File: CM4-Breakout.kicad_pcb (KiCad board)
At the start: 2 copper layers, 9 parts, among them J1 Conn_01x35_Male, J2 Conn_01x33_Male, J3 Conn_01x33_Male, J4 Conn_01x35_Male, J5 Conn_01x02_Female, J6 Conn_01x04_Male

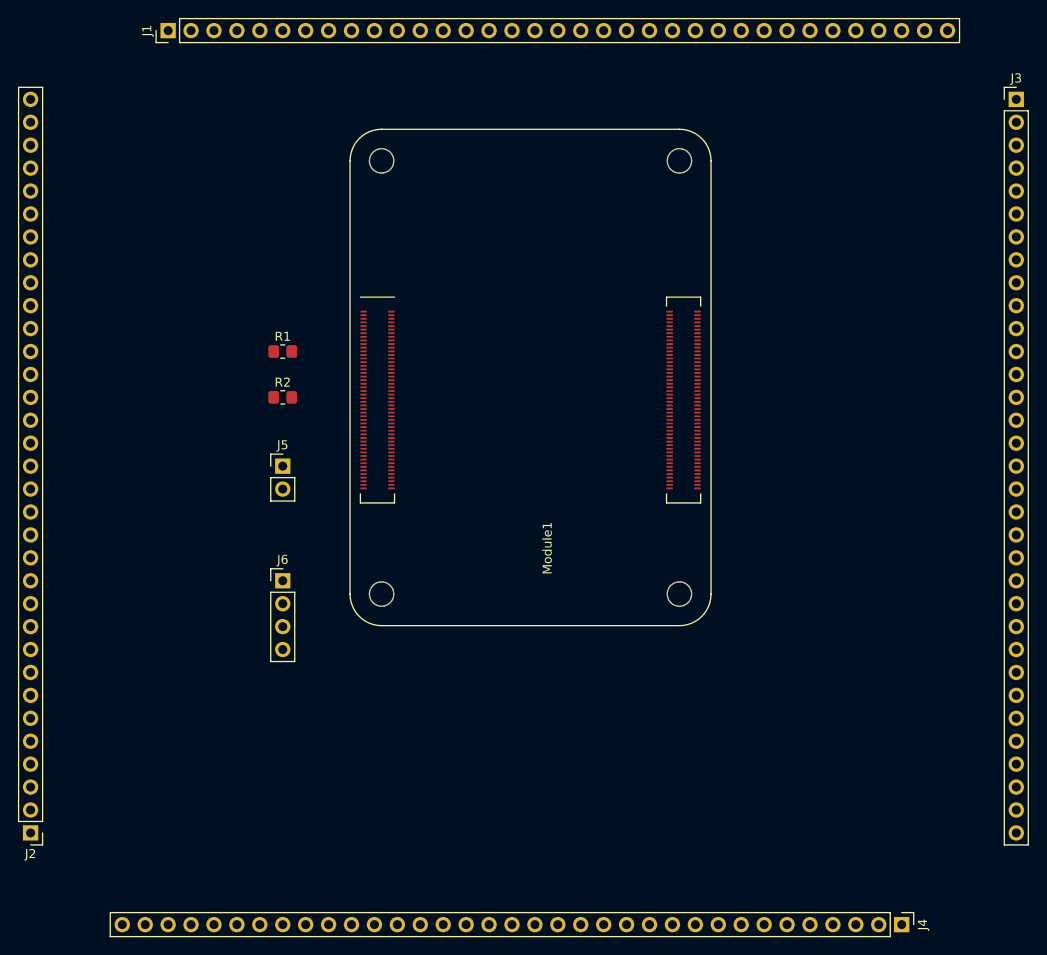
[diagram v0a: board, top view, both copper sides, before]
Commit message: Some updates to the pinout
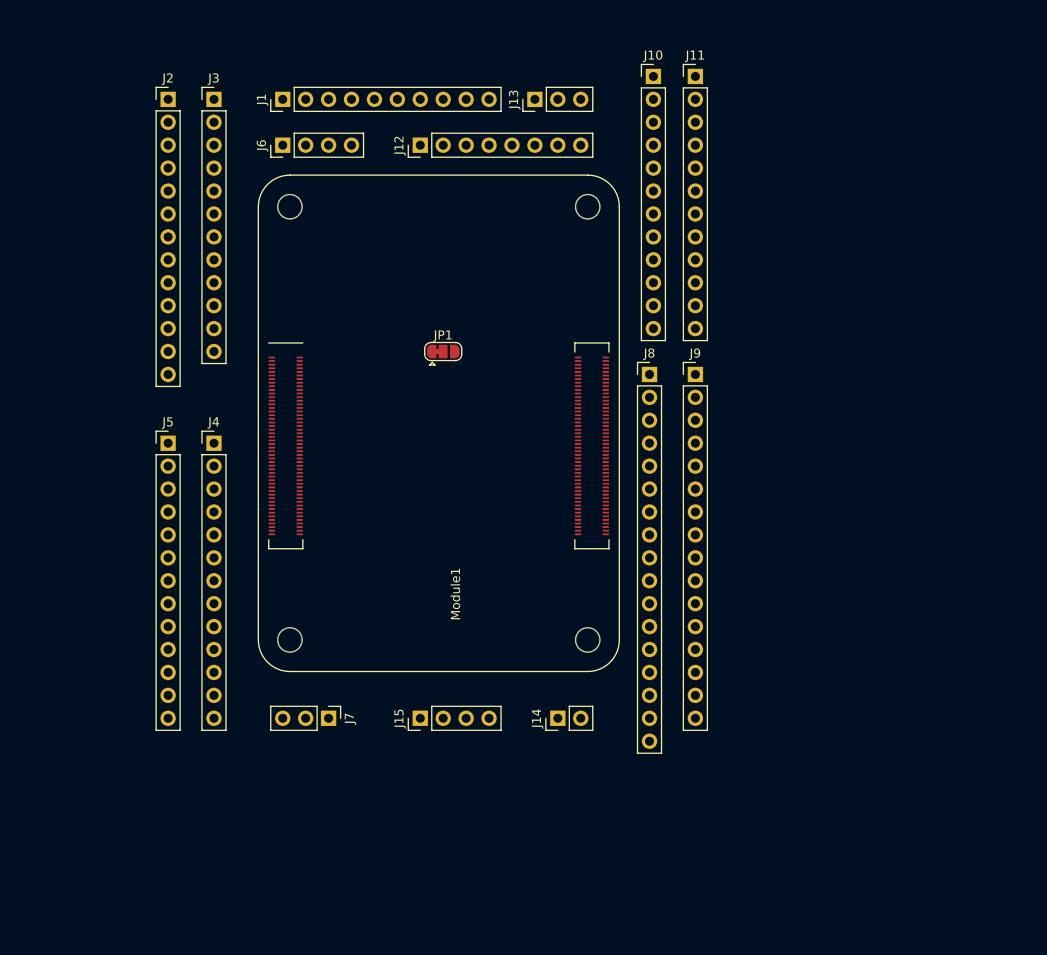
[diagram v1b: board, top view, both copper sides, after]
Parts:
- removed R1: 0R, Resistor_SMD:R_0805_2012Metric_Pad1.20x1.40mm_HandSolder
- removed R2: nf, Resistor_SMD:R_0805_2012Metric_Pad1.20x1.40mm_HandSolder
- added J10: Conn_01x12_Male, Connector_PinHeader_2.54mm:PinHeader_1x12_P2.54mm_Vertical, F.Cu at (178.2, 55.9)
- added J11: Conn_01x12_Male, Connector_PinHeader_2.54mm:PinHeader_1x12_P2.54mm_Vertical, F.Cu at (182.9, 55.9)
- added J12: Conn_01x08_Male, Connector_PinHeader_2.54mm:PinHeader_1x08_P2.54mm_Vertical, F.Cu at (152.4, 63.5)
- added J13: Conn_01x03_Male, Connector_PinHeader_2.54mm:PinHeader_1x03_P2.54mm_Vertical, F.Cu at (165.1, 58.4)
- added J14: Conn_01x02_Female, Connector_PinHeader_2.54mm:PinHeader_1x02_P2.54mm_Vertical, F.Cu at (167.6, 127.0)
- added J15: Conn_01x04_Male, Connector_PinHeader_2.54mm:PinHeader_1x04_P2.54mm_Vertical, F.Cu at (152.4, 127.0)
- added J7: Conn_01x03_Male, Connector_PinHeader_2.54mm:PinHeader_1x03_P2.54mm_Vertical, F.Cu at (142.2, 127.0)
- added J8: Conn_01x17_Male, Connector_PinHeader_2.54mm:PinHeader_1x17_P2.54mm_Vertical, F.Cu at (177.8, 88.9)
- added J9: Conn_01x16_Male, Connector_PinHeader_2.54mm:PinHeader_1x16_P2.54mm_Vertical, F.Cu at (182.9, 88.9)
- added JP1: SolderJumper_3_Bridged12, Jumper:SolderJumper-3_P1.3mm_Bridged12_RoundedPad1.0x1.5mm, F.Cu at (154.9, 86.4)
- J1: value Conn_01x35_Male -> Conn_01x10_Male; footprint Connector_PinHeader_2.54mm:PinHeader_1x35_P2.54mm_Vertical -> Connector_PinHeader_2.54mm:PinHeader_1x10_P2.54mm_Vertical
- J2: value Conn_01x33_Male -> Conn_01x13_Male; footprint Connector_PinHeader_2.54mm:PinHeader_1x33_P2.54mm_Vertical -> Connector_PinHeader_2.54mm:PinHeader_1x13_P2.54mm_Vertical
- J3: value Conn_01x33_Male -> Conn_01x12_Male; footprint Connector_PinHeader_2.54mm:PinHeader_1x33_P2.54mm_Vertical -> Connector_PinHeader_2.54mm:PinHeader_1x12_P2.54mm_Vertical
- J4: value Conn_01x35_Male -> Conn_01x13_Male; footprint Connector_PinHeader_2.54mm:PinHeader_1x35_P2.54mm_Vertical -> Connector_PinHeader_2.54mm:PinHeader_1x13_P2.54mm_Vertical
- J5: value Conn_01x02_Female -> Conn_01x13_Male; footprint Connector_PinHeader_2.54mm:PinHeader_1x02_P2.54mm_Vertical -> Connector_PinHeader_2.54mm:PinHeader_1x13_P2.54mm_Vertical
- moved J4 93.0 mm to (129.5, 96.5), turned to 0 degrees
- moved J3 88.9 mm to (129.5, 58.4)
- moved J2 82.7 mm to (124.5, 58.4), turned to 0 degrees
- moved J6 48.3 mm to (137.2, 63.5), turned to 90 degrees
- moved J1 14.8 mm to (137.2, 58.4)
- moved J5 13.0 mm to (124.5, 96.5)
- moved Module1 11.4 mm to (138.0, 118.3)
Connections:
- J2 pad 1: /PI_LED_nPWR -> /Ethernet_Pair0_P
- J2 pad 10: /GPIO8 -> /Ethernet_nLED2
- J2 pad 11: /GPIO9 -> /Ethernet_nLED3
- J2 pad 12: /GPIO10 -> /Ethernet_SYNC_IN
- J2 pad 13: /GPIO11 -> /Ethernet_SYNC_OUT
- J2 pad 2: /Pi_nLED_Activity -> /Ethernet_Pair0_N
- J2 pad 3: /GPIO_VREF -> /Ethernet_Pair1_P
- J2 pad 4: /GPIO2 -> /Ethernet_Pair1_N
- J2 pad 5: /GPIO3 -> /Ethernet_Pair2_P
- J2 pad 6: /GPIO4 -> /Ethernet_Pair2_N
- J2 pad 7: /GPIO5 -> /Ethernet_Pair3_P
- J2 pad 8: /GPIO6 -> /Ethernet_Pair3_N
- J2 pad 9: /GPIO7 -> /Ethernet_nLED1
- J3 pad 1: /CAM0_C_N -> /SD_CLK
- J3 pad 10: /CAM1_D0_P -> /SD_DAT7
- J3 pad 11: /CAM1_D1_N -> /SD_VDD_Override
- J3 pad 12: /CAM1_D1_P -> /SD_PWR_ON
- J3 pad 2: /CAM0_C_P -> /SD_CMD
- J3 pad 3: /CAM0_D0_N -> /SD_DAT0
- J3 pad 4: /CAM0_D0_P -> /SD_DAT1
- J3 pad 5: /CAM0_D1_N -> /SD_DAT2
- J3 pad 6: /CAM0_D1_P -> /SD_DAT3
- J3 pad 7: /CAM1_C_N -> /SD_DAT4
- J3 pad 8: /CAM1_C_P -> /SD_DAT5
- J3 pad 9: /CAM1_D0_N -> /SD_DAT6
- J4 pad 1: /HDMI0_CEC -> /GPIO15
- J4 pad 10: /HDMI0_TX1_P -> /GPIO24
- J4 pad 11: /HDMI0_TX2_N -> /GPIO25
- J4 pad 12: /HDMI0_TX2_P -> /GPIO26
- J4 pad 13: /HDMI1_CEC -> /GPIO27
- J4 pad 2: /HDMI0_CLK_N -> /GPIO16
- J4 pad 3: /HDMI0_CLK_P -> /GPIO17
- J4 pad 4: /HDMI0_HOTPLUG -> /GPIO18
- J4 pad 5: /HDMI0_SCL -> /GPIO19
- J4 pad 6: /HDMI0_SDA -> /GPIO20
- J4 pad 7: /HDMI0_TX0_N -> /GPIO21
- J4 pad 8: /HDMI0_TX0_P -> /GPIO22
- J4 pad 9: /HDMI0_TX1_N -> /GPIO23
- J5 pad 1: /+5v -> /GPIO2
- J5 pad 2: /GND -> /GPIO3
- J6 pad 1: /+5v -> /ID_SC
- J6 pad 2: /+3.3v -> /ID_SD
- J6 pad 3: /+1.8v -> /SCL0
- J6 pad 4: /GND -> /SDA0

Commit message: Final
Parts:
- added J16: Conn_01x03_Male, Connector_PinHeader_2.54mm:PinHeader_1x03_P2.54mm_Vertical, F.Cu at (185.0, 127.4)
- added J17: Conn_01x02_Female, Connector_PinHeader_2.54mm:PinHeader_1x02_P2.54mm_Vertical, F.Cu at (120.0, 140.0)
- added J18: Conn_01x04_Male, Connector_PinHeader_2.54mm:PinHeader_1x04_P2.54mm_Vertical, F.Cu at (167.5, 127.5)
- J10: value Conn_01x12_Male -> Conn_01x10_Male; footprint Connector_PinHeader_2.54mm:PinHeader_1x12_P2.54mm_Vertical -> Connector_PinHeader_2.54mm:PinHeader_1x10_P2.54mm_Vertical
- J11: value Conn_01x12_Male -> Conn_01x06_Male; footprint Connector_PinHeader_2.54mm:PinHeader_1x12_P2.54mm_Vertical -> Connector_PinHeader_2.54mm:PinHeader_1x06_P2.54mm_Vertical
- J12: value Conn_01x08_Male -> Conn_01x10_Male; footprint Connector_PinHeader_2.54mm:PinHeader_1x08_P2.54mm_Vertical -> Connector_PinHeader_2.54mm:PinHeader_1x10_P2.54mm_Vertical
- J13: value Conn_01x03_Male -> Conn_01x12_Male; footprint Connector_PinHeader_2.54mm:PinHeader_1x03_P2.54mm_Vertical -> Connector_PinHeader_2.54mm:PinHeader_1x12_P2.54mm_Vertical
- J14: value Conn_01x02_Female -> Conn_01x12_Male; footprint Connector_PinHeader_2.54mm:PinHeader_1x02_P2.54mm_Vertical -> Connector_PinHeader_2.54mm:PinHeader_1x12_P2.54mm_Vertical
- J15: value Conn_01x04_Male -> Conn_01x08_Male; footprint Connector_PinHeader_2.54mm:PinHeader_1x04_P2.54mm_Vertical -> Connector_PinHeader_2.54mm:PinHeader_1x08_P2.54mm_Vertical
- J8: value Conn_01x17_Male -> Conn_01x01_Male; footprint Connector_PinHeader_2.54mm:PinHeader_1x17_P2.54mm_Vertical -> Connector_PinHeader_2.54mm:PinHeader_1x01_P2.54mm_Vertical
- J9: value Conn_01x16_Male -> Conn_01x06_Male; footprint Connector_PinHeader_2.54mm:PinHeader_1x16_P2.54mm_Vertical -> Connector_PinHeader_2.54mm:PinHeader_1x06_P2.54mm_Vertical
- moved J12 71.9 mm to (205.0, 112.5), turned to 0 degrees
- moved J15 61.1 mm to (185.0, 75.3), turned to 180 degrees
- moved J10 59.1 mm to (195.0, 112.5)
- moved J14 56.2 mm to (205.0, 85.0), turned to 180 degrees
- moved J8 46.7 mm to (185.0, 135.0)
- moved JP1 43.8 mm to (140.0, 127.5)
- moved J11 42.8 mm to (205.0, 92.5)
- moved J13 29.9 mm to (195.0, 57.4), turned to 0 degrees
- moved J1 15.4 mm to (152.5, 57.5)
- moved J7 15.3 mm to (157.5, 127.5)
- moved J9 12.6 mm to (195.0, 92.5)
- moved J3 9.58 mm to (120.0, 57.5)
- moved J6 6.00 mm to (137.2, 57.5)
- moved J5 4.46 mm to (120.0, 96.5)
- moved J2 3.01 mm to (127.3, 57.4)
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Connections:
- net Net-(Module1-Pad104) renamed no_connect_141
- net Net-(Module1-Pad106) renamed no_connect_142
- net Net-(Module1-Pad76) renamed no_connect_143
- J10 pad 1: /HDMI0_CEC -> /CAM1_C_N
- J10 pad 10: /HDMI0_TX1_P -> /CAM1_D3_P
- J10 pad 2: /HDMI0_CLK_N -> /CAM1_C_P
- J10 pad 3: /HDMI0_CLK_P -> /CAM1_D0_N
- J10 pad 4: /HDMI0_HOTPLUG -> /CAM1_D0_P
- J10 pad 5: /HDMI0_SCL -> /CAM1_D1_N
- J10 pad 6: /HDMI0_SDA -> /CAM1_D1_P
- J10 pad 7: /HDMI0_TX0_N -> /CAM1_D2_N
- J10 pad 8: /HDMI0_TX0_P -> /CAM1_D2_P
- J10 pad 9: /HDMI0_TX1_N -> /CAM1_D3_N
- J11 pad 1: /HDMI1_CEC -> /DSI0_C_N
- J11 pad 2: /HDMI1_CLK_N -> /DSI0_C_P
- J11 pad 3: /HDMI1_CLK_P -> /DSI0_D0_N
- J11 pad 4: /HDMI1_HOTPLUG -> /DSI0_D0_P
- J11 pad 5: /HDMI1_SCL -> /DSI0_D1_N
- J11 pad 6: /HDMI1_SDA -> /DSI0_D1_P
- J12 pad 1: /PCIe_CLK_nREQ -> /DSI1_C_N
- J12 pad 2: /PCIe_CLK_N -> /DSI1_C_P
- J12 pad 3: /PCIe_CLK_P -> /DSI1_D0_N
- J12 pad 4: /PCIe_nRST -> /DSI1_D0_P
- J12 pad 5: /PCIe_RX_N -> /DSI1_D1_N
- J12 pad 6: /PCIe_RX_P -> /DSI1_D1_P
- J12 pad 7: /PCIe_TX_N -> /DSI1_D2_N
- J12 pad 8: /PCIe_TX_P -> /DSI1_D2_P
- J13 pad 1: /USB_OTG_ID -> /HDMI0_CEC
- J13 pad 2: /USB2_N -> /HDMI0_CLK_N
- J13 pad 3: /USB2_P -> /HDMI0_CLK_P
- J14 pad 1: /+5v -> /HDMI1_CEC
- J14 pad 2: /GND -> /HDMI1_CLK_N
- J15 pad 1: /+5v -> /PCIe_CLK_nREQ
- J15 pad 2: /+3.3v -> /PCIe_CLK_N
- J15 pad 3: /+1.8v -> /PCIe_CLK_P
- J15 pad 4: /GND -> /PCIe_nRST
- J8 pad 1: /DSI0_C_N -> /VDAC_COMP
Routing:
- net /Pi_nLED_Activity: track 0.00 -> 86.4 mm
- net /AnalogIP1: track 0.00 -> 78.2 mm
- net /nRPIBOOT: track 0.00 -> 72.6 mm, vias 0 -> 2
- net /Camera_GPIO: track 0.00 -> 71.3 mm
- net /Global_EN: track 0.00 -> 68.5 mm
- net /USB_OTG_ID: track 0.00 -> 60.1 mm
- net /SCL0: track 0.00 -> 58.5 mm, vias 0 -> 2
- net /nEXTRST: track 0.00 -> 58.2 mm
- net /USB2_P: track 0.00 -> 56.5 mm
- net /USB2_N: track 0.00 -> 56.5 mm
- net /GPIO11: track 0.00 -> 56.3 mm, vias 0 -> 2
- net /+5v: track 0.00 -> 52.7 mm
- net /GPIO12: track 0.00 -> 51.6 mm, vias 0 -> 1
- net /GPIO26: track 0.00 -> 47.0 mm, vias 0 -> 2
- net /GPIO10: track 0.00 -> 46.5 mm, vias 0 -> 2
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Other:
- board outline added: 95 x 95 mm
